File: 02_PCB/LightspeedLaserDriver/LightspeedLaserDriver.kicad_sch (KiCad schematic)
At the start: 9 parts, among them J1 Conn_01x02_Pin, J2 SMA, J3 Conn_01x02_Pin, J4 SMA

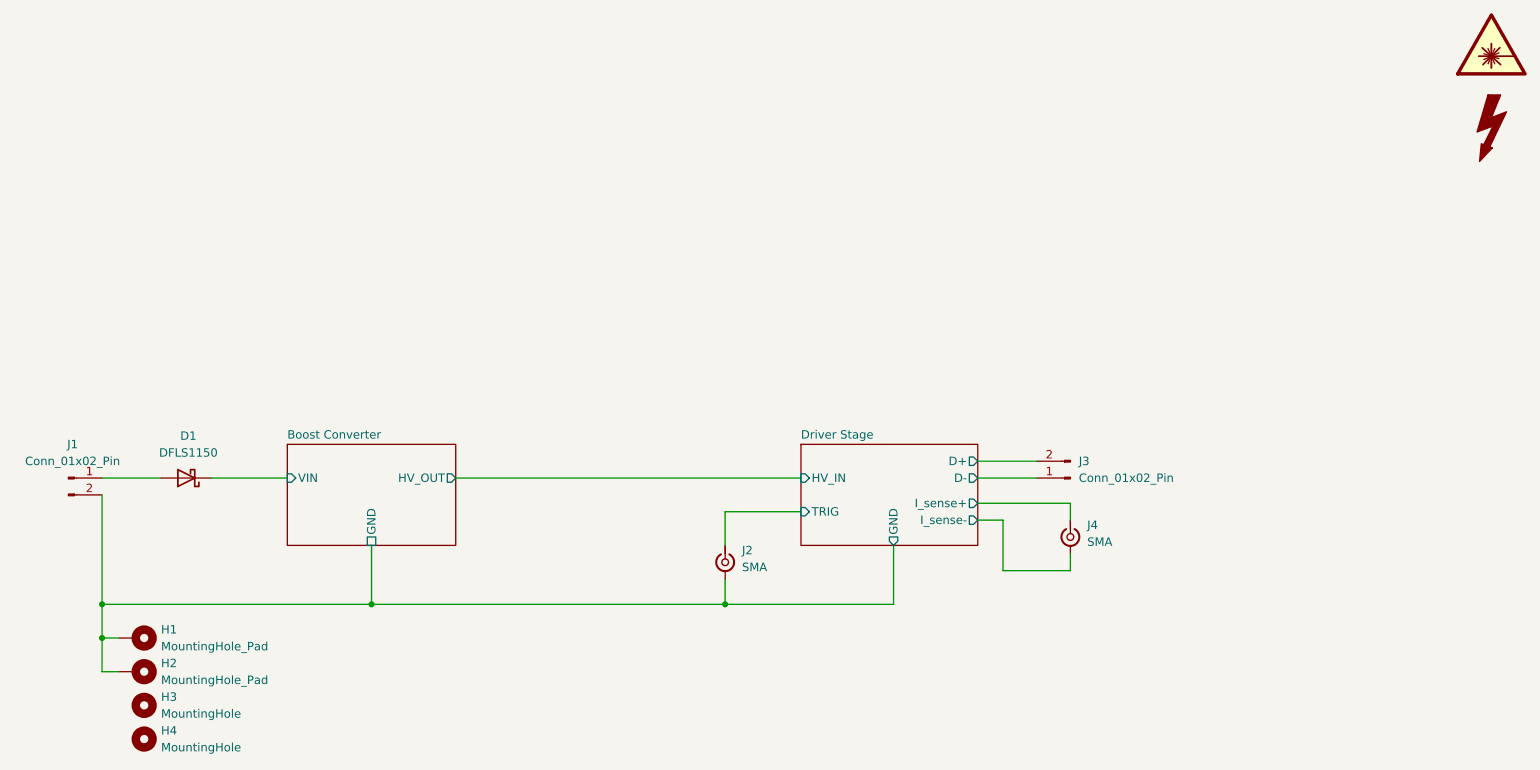
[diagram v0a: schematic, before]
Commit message: feat(pcb): add peripherals to PCB
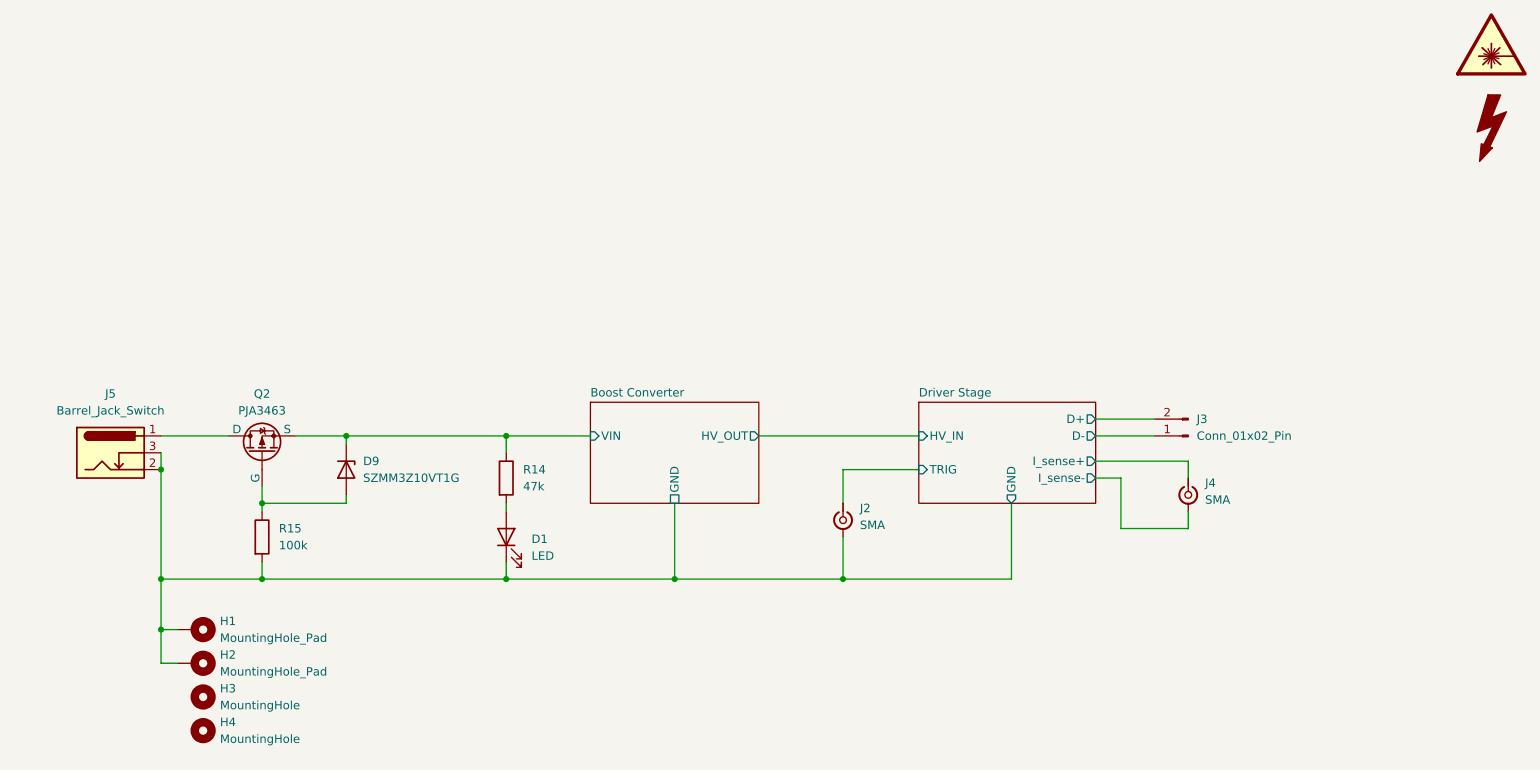
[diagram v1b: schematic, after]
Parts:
- removed D1: DFLS1150, Diode_SMD:D_PowerDI-123, symbol Device:D_Schottky
- removed J1: Conn_01x02_Pin, Connector_PinHeader_2.54mm:PinHeader_1x02_P2.54mm_Vertical, symbol Connector:Conn_01x02_Pin
- added D1: LED, LED_SMD:LED_0603_1608Metric, symbol Device:LED
- added D9: SZMM3Z10VT1G, Diode_SMD:D_SOD-323, symbol Device:D_Zener
- added J5: Barrel_Jack_Switch, Connector_BarrelJack:BarrelJack_Wuerth_694106106102_2.0x5.5mm, symbol Connector:Barrel_Jack_Switch
- added Q2: PJA3463, Package_TO_SOT_SMD:SOT-23, symbol Simulation_SPICE:PMOS
- added R14: 47k, Resistor_SMD:R_0603_1608Metric, symbol Device:R
- added R15: 100k, Resistor_SMD:R_0603_1608Metric, symbol Device:R
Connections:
- net Boost Converter/GND: now also D1.1 (K), J5.2, J5.3, R15.2
- net Boost Converter/VIN: now also D9.1 (K), Q2.3 (S), R14.1
- new net: D1.2 (A), R14.2
- new net: J5.1, Q2.1 (D)
- new net: D9.2 (A), Q2.2 (G), R15.1
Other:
- moved on the sheet: H1, H2, H3, H4, J2, J3, J4

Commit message: feat(pcb): route all traces
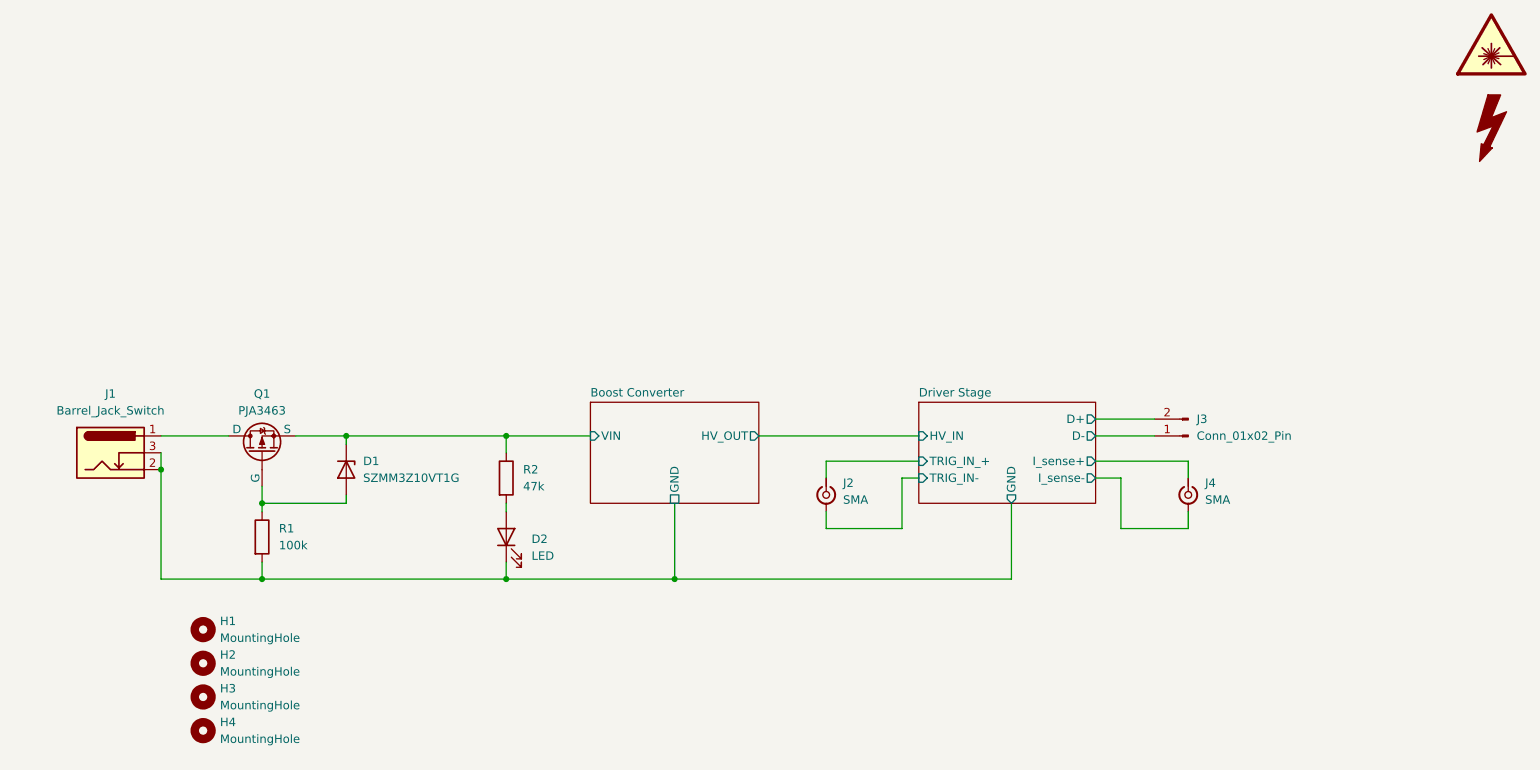
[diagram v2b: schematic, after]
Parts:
- removed H1, H2: MountingHole_Pad, MountingHole:MountingHole_3.2mm_M3_Pad_Via, symbol Mechanical:MountingHole_Pad
- added H1, H2: MountingHole, MountingHole:MountingHole_3.2mm_M3, symbol Mechanical:MountingHole
- J2, J4: footprint Connector_Coaxial:SMA_Molex_73251-2200_Horizontal -> Connector_Coaxial:SMA_Wurth_60312002114503_Vertical
- renumbered D9 to D1, D1 to D2, J5 to J1, Q2 to Q1, R15 to R1, R14 to R2
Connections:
- net Boost Converter/GND: no longer J2.2 (Ext)
- net Driver Stage/TRIG renamed Driver Stage/TRIG_IN_+
- new net Driver Stage/TRIG_IN-: J2.2 (Ext)
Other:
- sheet Driver Stage ports: added TRIG_IN-, TRIG_IN_+; removed TRIG
- moved on the sheet: J2

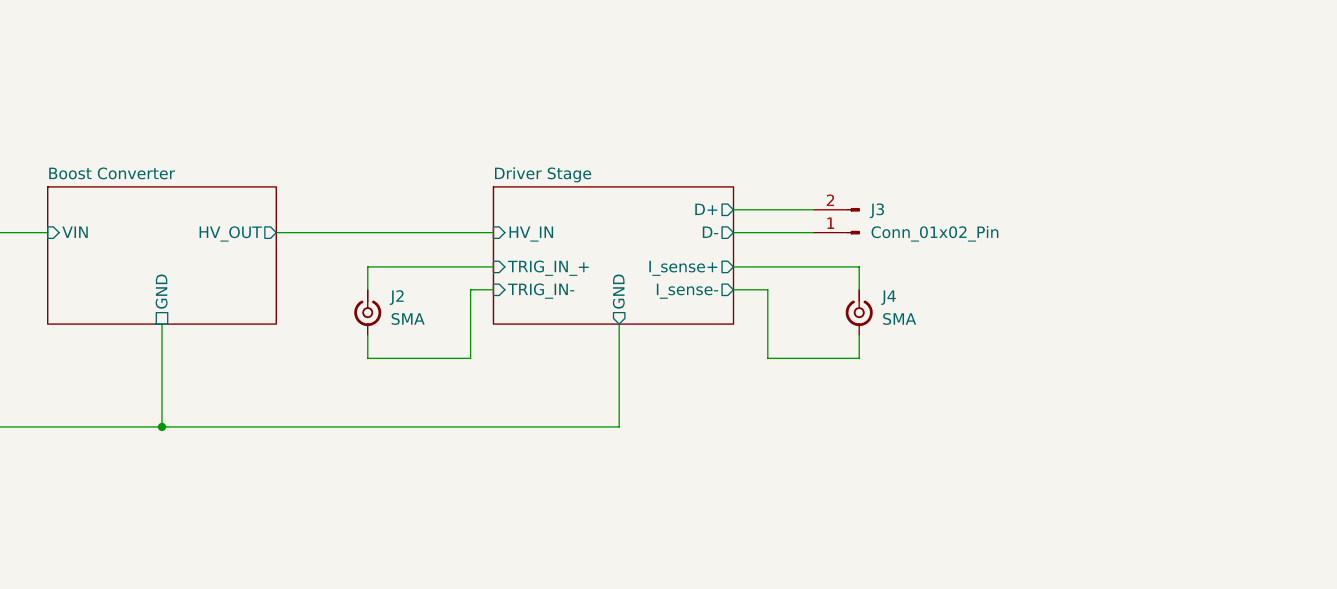
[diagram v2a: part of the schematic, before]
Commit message: feat(pcb): laser driver layout draft finished, add high voltage indicator LED and discharge path
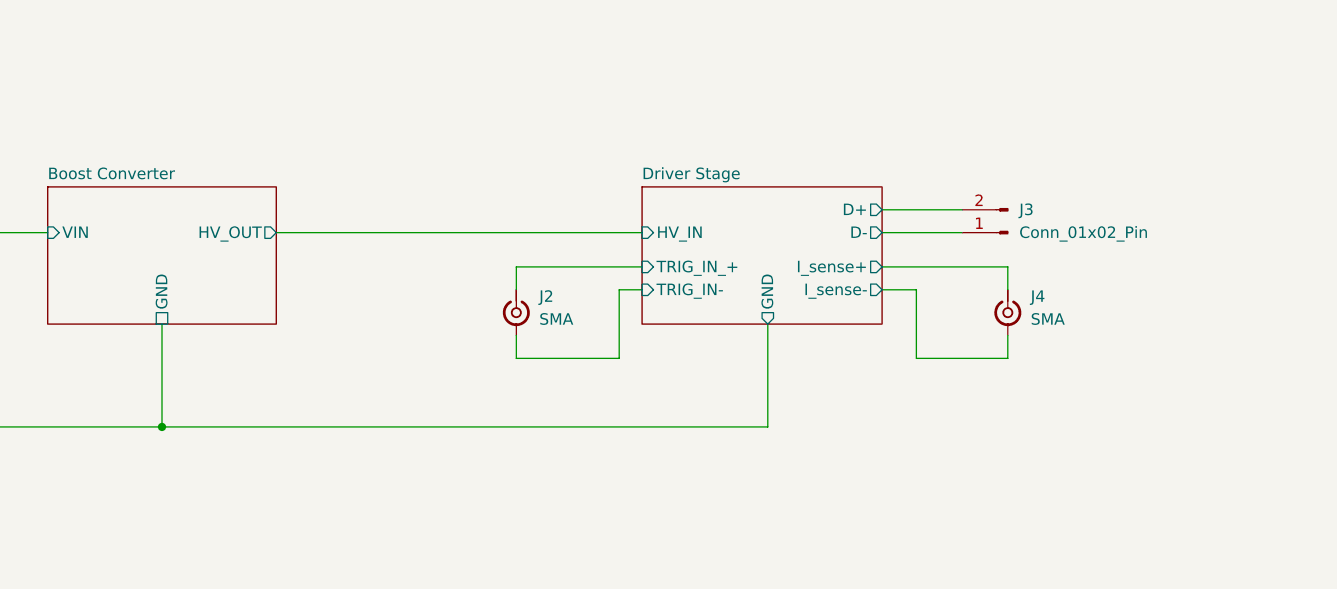
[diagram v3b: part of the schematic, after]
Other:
- moved on the sheet: J2, J3, J4
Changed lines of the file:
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@@
 	(wire
 		(pts
-			(xy 224.79 77.47) (xy 215.9 77.47)
+			(xy 241.3 77.47) (xy 232.41 77.47)
 		)
 		(stroke
@@
 	(wire
 		(pts
-			(xy 186.69 93.98) (xy 186.69 86.36)
+			(xy 203.2 93.98) (xy 203.2 86.36)
 		)
 		(stroke
@@
 	(wire
 		(pts
-			(xy 229.87 83.82) (xy 215.9 83.82)
-		)
-		(stroke
-			(width 0)
-			(type default)
-		)
-	)
-	(wire
-		(pts
-			(xy 215.9 86.36) (xy 219.71 86.36)
+			(xy 246.38 83.82) (xy 232.41 83.82)
+		)
+		(stroke
+			(width 0)
+			(type default)
+		)
+	)
+	(wire
+		(pts
+			(xy 232.41 86.36) (xy 236.22 86.36)
 		)
 		(stroke
@@
 	(wire
 		(pts
-			(xy 175.26 91.44) (xy 175.26 93.98)
+			(xy 191.77 91.44) (xy 191.77 93.98)
 		)
 		(stroke
@@
 	(wire
 		(pts
-			(xy 219.71 93.98) (xy 229.87 93.98)
-		)
-		(stroke
-			(width 0)
-			(type default)
-		)
-	)
-	(wire
-		(pts
-			(xy 152.4 101.6) (xy 203.2 101.6)
+			(xy 236.22 93.98) (xy 246.38 93.98)
+		)
+		(stroke
+			(width 0)
+			(type default)
+		)
+	)
+	(wire
+		(pts
+			(xy 152.4 101.6) (xy 219.71 101.6)
+		)
+		(stroke
+			(width 0)
+			(type default)
+		)
+	)
+	(wire
+		(pts
+			(xy 165.1 80.01) (xy 205.74 80.01)
 		)
 		(stroke
@@
 	(wire
 		(pts
-			(xy 175.26 93.98) (xy 186.69 93.98)
+			(xy 191.77 93.98) (xy 203.2 93.98)
 		)
 		(stroke
@@
 	(wire
 		(pts
-			(xy 229.87 86.36) (xy 229.87 83.82)
+			(xy 246.38 86.36) (xy 246.38 83.82)
 		)
 		(stroke
@@
 	(wire
 		(pts
-			(xy 186.69 86.36) (xy 189.23 86.36)
+			(xy 203.2 86.36) (xy 205.74 86.36)
 		)
 		(stroke
@@
 	(wire
 		(pts
-			(xy 219.71 86.36) (xy 219.71 93.98)
+			(xy 236.22 86.36) (xy 236.22 93.98)
 		)
 		(stroke
@@
 	(wire
 		(pts
-			(xy 175.26 86.36) (xy 175.26 83.82)
-		)
-		(stroke
-			(width 0)
-			(type default)
-		)
-	)
-	(wire
-		(pts
-			(xy 203.2 90.17) (xy 203.2 101.6)
+			(xy 191.77 86.36) (xy 191.77 83.82)
+		)
+		(stroke
+			(width 0)
+			(type default)
+		)
+	)
+	(wire
+		(pts
+			(xy 219.71 90.17) (xy 219.71 101.6)
 		)
 		(stroke
@@
 	(wire
 		(pts
-			(xy 175.26 83.82) (xy 189.23 83.82)
-		)
-		(stroke
-			(width 0)
-			(type default)
-		)
-	)
-	(wire
-		(pts
-			(xy 215.9 80.01) (xy 224.79 80.01)
-		)
-		(stroke
-			(width 0)
-			(type default)
-		)
-	)
-	(wire
-		(pts
-			(xy 229.87 93.98) (xy 229.87 91.44)
+			(xy 191.77 83.82) (xy 205.74 83.82)
+		)
+		(stroke
+			(width 0)
+			(type default)
+		)
+	)
+	(wire
+		(pts
+			(xy 232.41 80.01) (xy 241.3 80.01)
+		)
+		(stroke
+			(width 0)
+			(type default)
+		)
+	)
+	(wire
+		(pts
+			(xy 246.38 93.98) (xy 246.38 91.44)
 		)
 		(stroke
@@
 		(pts
 			(xy 102.87 80.01) (xy 127 80.01)
-		)
-		(stroke
-			(width 0)
-			(type default)
-		)
-	)
-	(wire
-		(pts
-			(xy 165.1 80.01) (xy 189.23 80.01)
 		)
 		(stroke
@@
 	(symbol
 		(lib_id "Connector:Conn_01x02_Pin")
-		(at 229.87 80.01 180)
+		(at 246.38 80.01 180)
 		(unit 1)
 		(exclude_from_sim no)
@@
 		(fields_autoplaced yes)
 		(property "Reference" "J3"
-			(at 231.14 77.4699 0)
+			(at 247.65 77.4699 0)
 			(effects
 				(font
@@
 		)
 		(property "Value" "Conn_01x02_Pin"
-			(at 231.14 80.0099 0)
+			(at 247.65 80.0099 0)
 			(effects
 				(font
@@
 		)
 		(property "Footprint" "Resistor_SMD:R_0815_2038Metric_Pad1.20x4.05mm_HandSolder"
-			(at 229.87 80.01 0)
+			(at 246.38 80.01 0)
 			(effects
 				(font
@@
 		)
 		(property "Datasheet" "~"
-			(at 229.87 80.01 0)
+			(at 246.38 80.01 0)
 			(effects
 				(font
@@
 		)
 		(property "Description" "Generic connector, single row, 01x02, script generated"
-			(at 229.87 80.01 0)
+			(at 246.38 80.01 0)
 			(effects
 				(font
@@
 	(symbol
 		(lib_id "Connector:Conn_Coaxial_Small")
-		(at 229.87 88.9 270)
+		(at 246.38 88.9 270)
 		(unit 1)
 		(exclude_from_sim no)
@@
 		(fields_autoplaced yes)
 		(property "Reference" "J4"
-			(at 232.41 87.1103 90)
+			(at 248.92 87.1103 90)
 			(effects
 				(font
@@
 		)
 		(property "Value" "SMA"
-			(at 232.41 89.6503 90)
+			(at 248.92 89.6503 90)
 			(effects
 				(font
@@
 		)
 		(property "Footprint" "Connector_Coaxial:SMA_Wurth_60312002114503_Vertical"
-			(at 229.87 88.9 0)
+			(at 246.38 88.9 0)
 			(effects
 				(font
@@
 		)
 		(property "Datasheet" "~"
-			(at 229.87 88.9 0)
+			(at 246.38 88.9 0)
 			(effects
 				(font
@@
 		)
 		(property "Description" "small coaxial connector (BNC, SMA, SMB, SMC, Cinch/RCA, LEMO, ...)"
-			(at 229.87 88.9 0)
+			(at 246.38 88.9 0)
 			(effects
 				(font
@@
 	(symbol
 		(lib_id "Connector:Conn_Coaxial_Small")
-		(at 175.26 88.9 270)
+		(at 191.77 88.9 270)
 		(unit 1)
 		(exclude_from_sim no)
@@
 		(fields_autoplaced yes)
 		(property "Reference" "J2"
-			(at 177.8 87.1103 90)
+			(at 194.31 87.1103 90)
 			(effects
 				(font
@@
 		)
 		(property "Value" "SMA"
-			(at 177.8 89.6503 90)
+			(at 194.31 89.6503 90)
 			(effects
 				(font
@@
 		)
 		(property "Footprint" "Connector_Coaxial:SMA_Wurth_60312002114503_Vertical"
-			(at 175.26 88.9 0)
+			(at 191.77 88.9 0)
 			(effects
 				(font
@@
 		)
 		(property "Datasheet" "~"
-			(at 175.26 88.9 0)
+			(at 191.77 88.9 0)
 			(effects
 				(font
@@
 		)
 		(property "Description" "small coaxial connector (BNC, SMA, SMB, SMC, Cinch/RCA, LEMO, ...)"
-			(at 175.26 88.9 0)
+			(at 191.77 88.9 0)
 			(effects
 				(font
@@
 	)
 	(sheet
-		(at 189.23 74.93)
+		(at 205.74 74.93)
 		(size 26.67 15.24)
 		(exclude_from_sim no)
@@
 		)
 		(property "Sheetname" "Driver Stage"
-			(at 189.23 74.2184 0)
+			(at 205.74 74.2184 0)
 			(effects
 				(font
@@
 		)
 		(property "Sheetfile" "DriverStage.kicad_sch"
-			(at 189.23 90.7546 0)
+			(at 205.74 90.7546 0)
 			(effects
 				(font
@@
 		)
 		(pin "GND" output
-			(at 203.2 90.17 270)
+			(at 219.71 90.17 270)
 			(effects
 				(font
@@
 		)
 		(pin "HV_IN" input
-			(at 189.23 80.01 180)
+			(at 205.74 80.01 180)
 			(effects
 				(font
@@
 		)
 		(pin "D+" output
-			(at 215.9 77.47 0)
+			(at 232.41 77.47 0)
 			(effects
 				(font
@@
 		)
 		(pin "D-" output
-			(at 215.9 80.01 0)
+			(at 232.41 80.01 0)
 			(effects
 				(font
@@
 		)
 		(pin "I_sense+" output
-			(at 215.9 83.82 0)
+			(at 232.41 83.82 0)
 			(effects
 				(font
@@
 		)
 		(pin "I_sense-" output
-			(at 215.9 86.36 0)
+			(at 232.41 86.36 0)
 			(effects
 				(font
@@
 		)
 		(pin "TRIG_IN-" input
-			(at 189.23 86.36 180)
+			(at 205.74 86.36 180)
 			(effects
 				(font
@@
 		)
 		(pin "TRIG_IN_+" input
-			(at 189.23 83.82 180)
-			(effects
-				(font
+			(at 205.74 83.82 180)
+			(effects
+				(font

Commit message: feat(pcb): improve the design draft
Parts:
- added F1: MFU0603FF03000, Fuse:Fuse_0603_1608Metric, symbol Device:Fuse
- D2: value LED -> APTD1608LCGCK
- J1: value Barrel_Jack_Switch -> 694106106102
- Q1: value PJA3463 -> PJA3463_R1_00001
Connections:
- net at J1.1: now also F1.1; no longer Q1.1 (D)
- new net: F1.2, Q1.1 (D)
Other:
- moved on the sheet: D1, D2, H1, H2, H3, H4, J1, J2, J3, J4, Q1, R1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

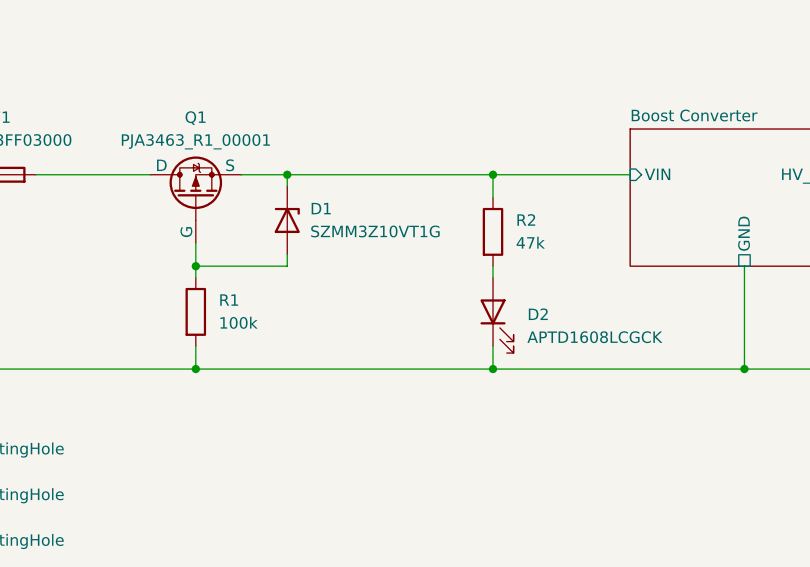
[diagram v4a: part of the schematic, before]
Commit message: feat(pcb): laser driver V0.1 as ordered on 08.03.2026
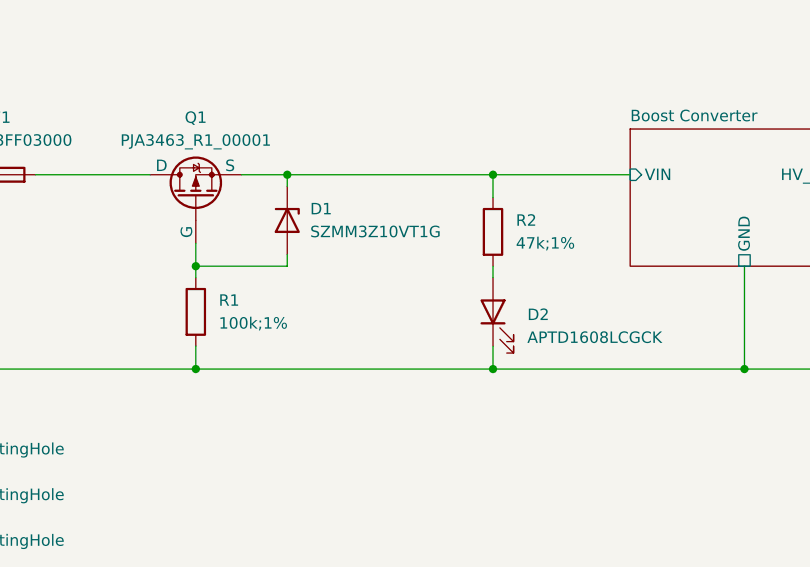
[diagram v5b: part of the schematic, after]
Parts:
- R1: value 100k -> 100k;1%
- R2: value 47k -> 47k;1%
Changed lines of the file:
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@@
 			)
 		)
-		(property "Value" "100k"
+		(property "Value" "100k;1%"
 			(at 106.68 96.5199 0)
 			(effects
@@
 			)
 		)
-		(property "Value" "47k"
+		(property "Value" "47k;1%"
 			(at 139.7 87.6299 0)
 			(effects
